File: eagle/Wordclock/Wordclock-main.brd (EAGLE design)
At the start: 50 x 50 mm, 36 parts, among them IC1 MEGA8-P, J1 AVR_SPI_PRG_6PTH, Q1 16MHz

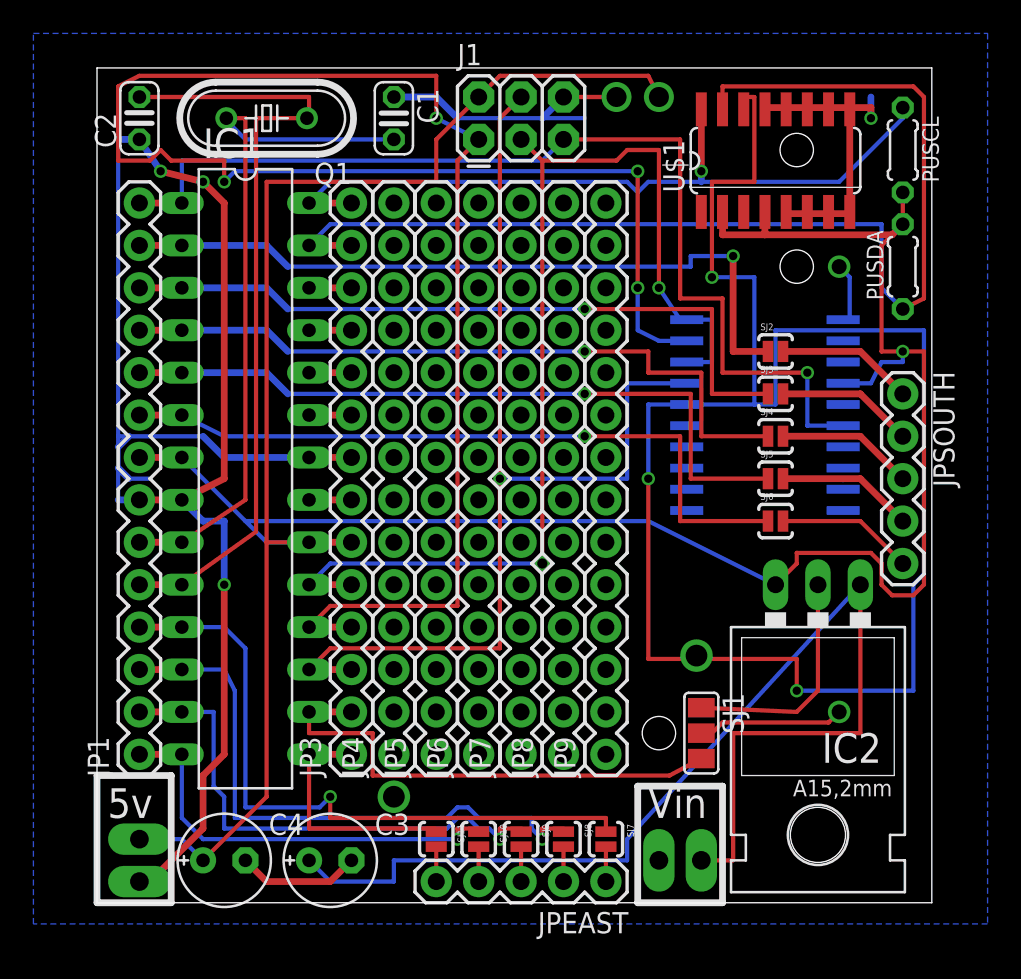
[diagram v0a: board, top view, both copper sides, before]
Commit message: Wordclock main : v1.1 with still wrong DS3231
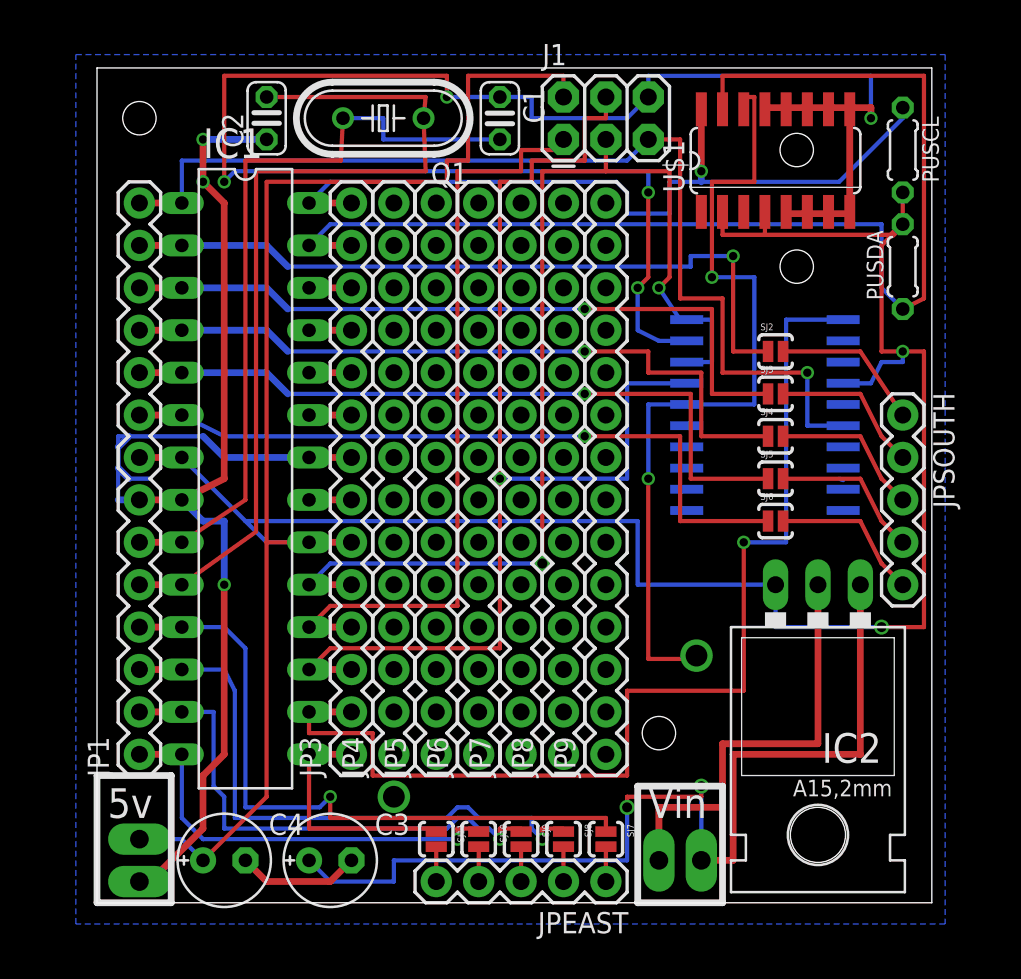
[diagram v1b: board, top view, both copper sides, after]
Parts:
- removed SJ1: (no value), SparkFun:SJ_2
- moved C2 7.62 mm to (10.2, 47.0)
- moved Q1 6.98 mm to (17.1, 47.0)
- moved C1 6.35 mm to (24.1, 47.0)
- moved J1 5.08 mm to (27.9, 45.7)
- moved JPSOUTH 1.27 mm to (48.3, 29.2)
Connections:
- removed net N$13: DS3234.19, IC1.18, J1.1, JP3.4
- removed net N$2: DS3234.1, SJ1.2
- new net S$1: IC1.18, J1.1, JP3.4
- net GND: now also DS3234.19; no longer SJ1.1
- net N$6: no longer SJ1.3
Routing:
- net N$13: track 115.5 -> 0.00 mm, vias 4 -> 0
- net GND: track 155.6 -> 222.7 mm, vias 5 -> 8
- net N$7: track 100.0 -> 48.3 mm, vias 3 -> 2
- net S$1: track 3.44 -> 46.2 mm, vias 1 -> 0
- net N$6: track 30.1 -> 65.4 mm, vias 0 -> 1
- net N$2: track 8.78 -> 0.00 mm, vias 1 -> 0
- net VIN: track 68.8 -> 60.2 mm, vias 0 -> 2
- net N$5: track 47.4 -> 53.7 mm
- net N$14: track 64.6 -> 70.4 mm
- net N$4: track 41.9 -> 46.4 mm
- net N$30: track 45.8 -> 48.7 mm
- net VCC: track 181.5 -> 183.3 mm
- net N$31: track 70.0 -> 71.7 mm
- net N$12: track 66.5 -> 65.3 mm
- net N$19: track 8.04 -> 9.08 mm
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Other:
- board text added: "Order #-----"
- board text added: "v1.1 (Feb2012)"
- board text removed: "- +"
- board text removed: "Order #42225"
- board text removed: "v1.0 (Jan2012)"

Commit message: v1.1 with corrected DS3231 package : a SO16W(ide)
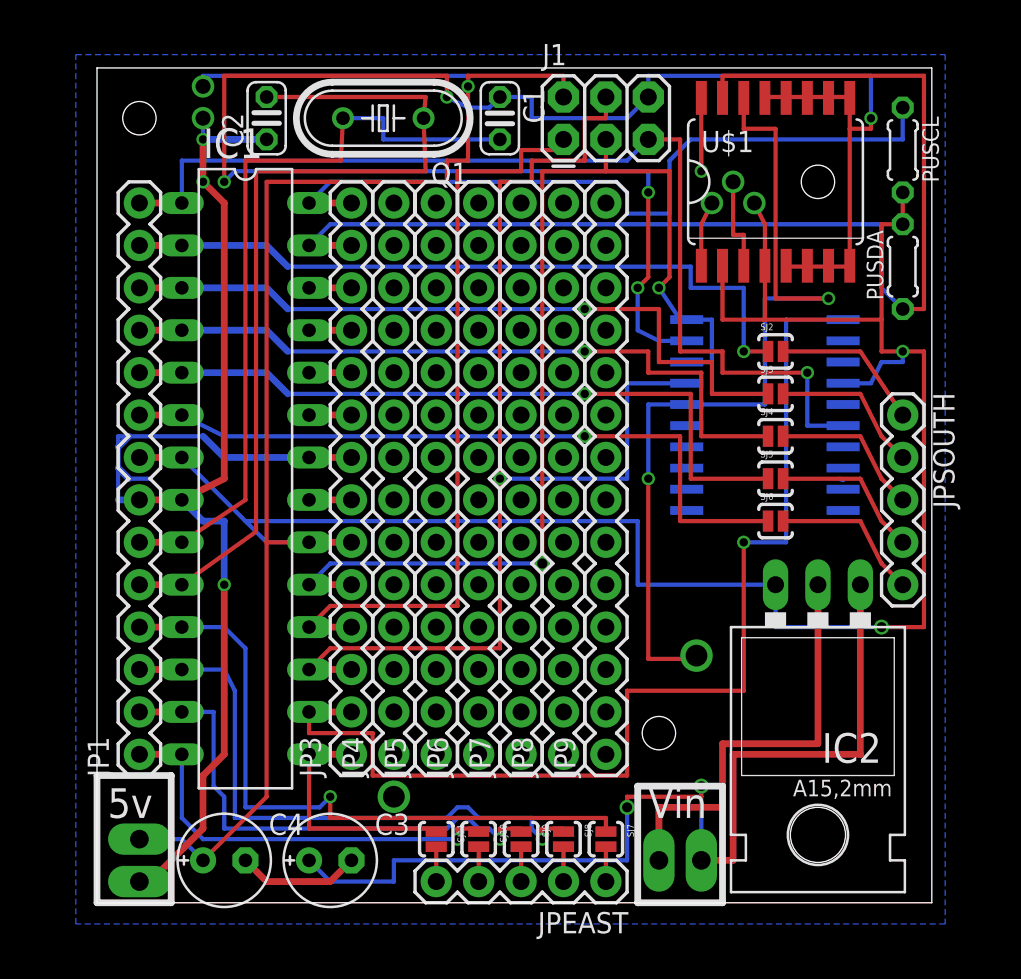
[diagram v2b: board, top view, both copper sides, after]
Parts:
- U$1: device DS3231:SO16 -> kalshagar:SO16W
- moved U$1 1.80 mm to (41.9, 43.2)
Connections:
- new net S$10: U$1.16
- new net S$11: U$1.10, U$1.11, U$1.9
- new net S$12: U$1.2, U$1.4
- new net S$7: U$1.12, U$1.13
- new net S$8: U$1.7, U$1.8
- new net S$9: U$1.5, U$1.6
- net GND: no longer U$1.10, U$1.11, U$1.12, U$1.13, U$1.5, U$1.6, U$1.7, U$1.8, U$1.9
- net N$30: no longer U$1.16
- net VCC: no longer U$1.2, U$1.4
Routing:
- net VCC: track 183.3 -> 209.0 mm, vias 2 -> 5
- net GND: track 222.7 -> 228.1 mm, vias 8 -> 9
- net S$14: track 0.00 -> 5.08 mm, vias 0 -> 1
- net S$16: track 0.00 -> 3.96 mm, vias 0 -> 1
- net N$7: track 48.3 -> 52.1 mm
- net N$30: track 48.7 -> 52.1 mm
- net N$20: track 44.3 -> 43.1 mm
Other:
- board text added: "Order #44009"
- board text removed: "Order #-----"

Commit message: BUGFIX v1.2 : fixed an horrible bug with DS3234 : pin 19 must not be grounded but linked to Atmegaxx8 pin 18 (PB4)
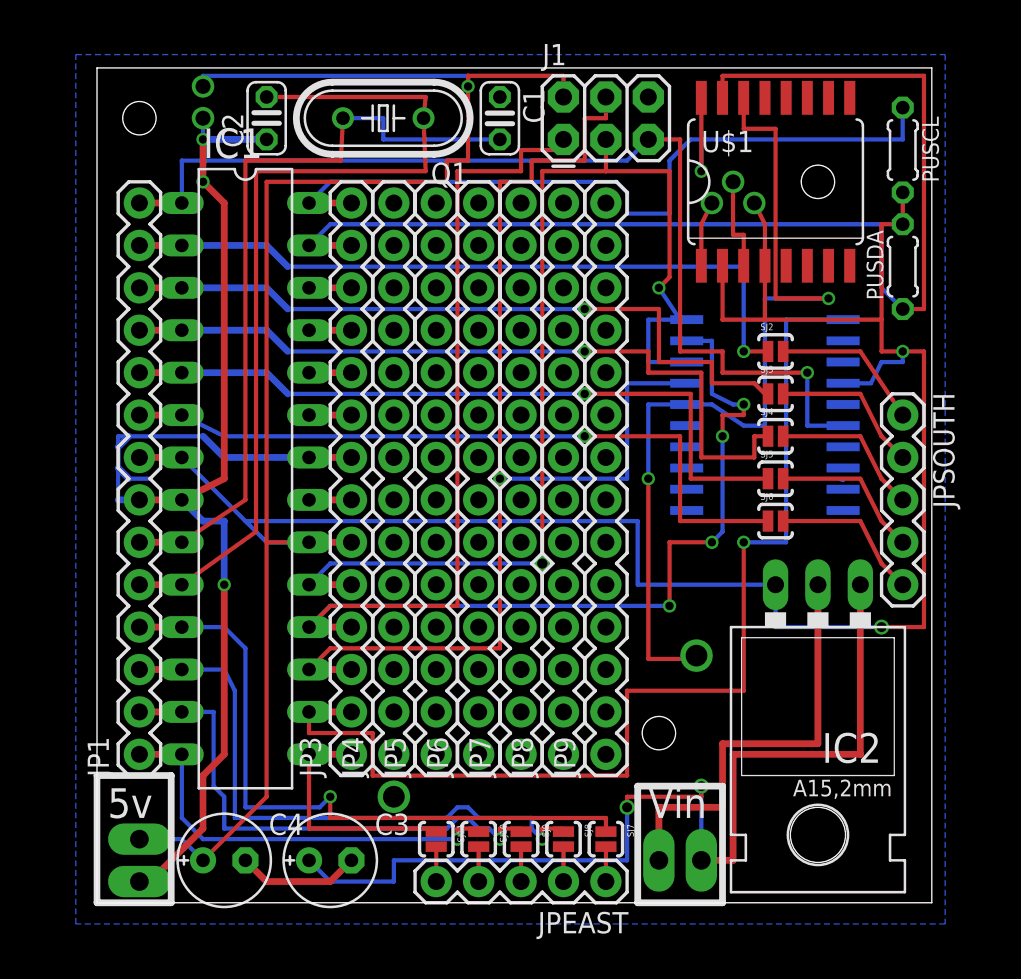
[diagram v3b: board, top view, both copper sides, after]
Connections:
- removed net S$1: IC1.18, J1.1, JP3.4
- new net S$13: DS3234.19, IC1.18, J1.1, JP3.4
- net GND: no longer DS3234.19
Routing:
- net GND: track 228.1 -> 116.0 mm, vias 9 -> 4
- net S$13: track 0.00 -> 91.0 mm, vias 0 -> 4
- net S$1: track 46.2 -> 0.00 mm
- net N$22: track 43.1 -> 45.6 mm
- net N$7: track 52.1 -> 53.7 mm
- net N$12: track 65.3 -> 66.6 mm
- net N$6: track 65.4 -> 66.0 mm
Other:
- board text added: "v1.2"
- board text added: "v1.2 (May2013)"
- board text removed: "v1.1 (Feb2012)"
